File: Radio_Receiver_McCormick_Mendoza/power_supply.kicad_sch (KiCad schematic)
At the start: 27 parts, among them J1 VBAT, J2 GND, J23 VDDA, J26 +5V, J3 VA_3.3, J36 +5V RAW, J37 V_4.8, J39 VDD, J4 VA_4.8, J6 Conn_01x02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

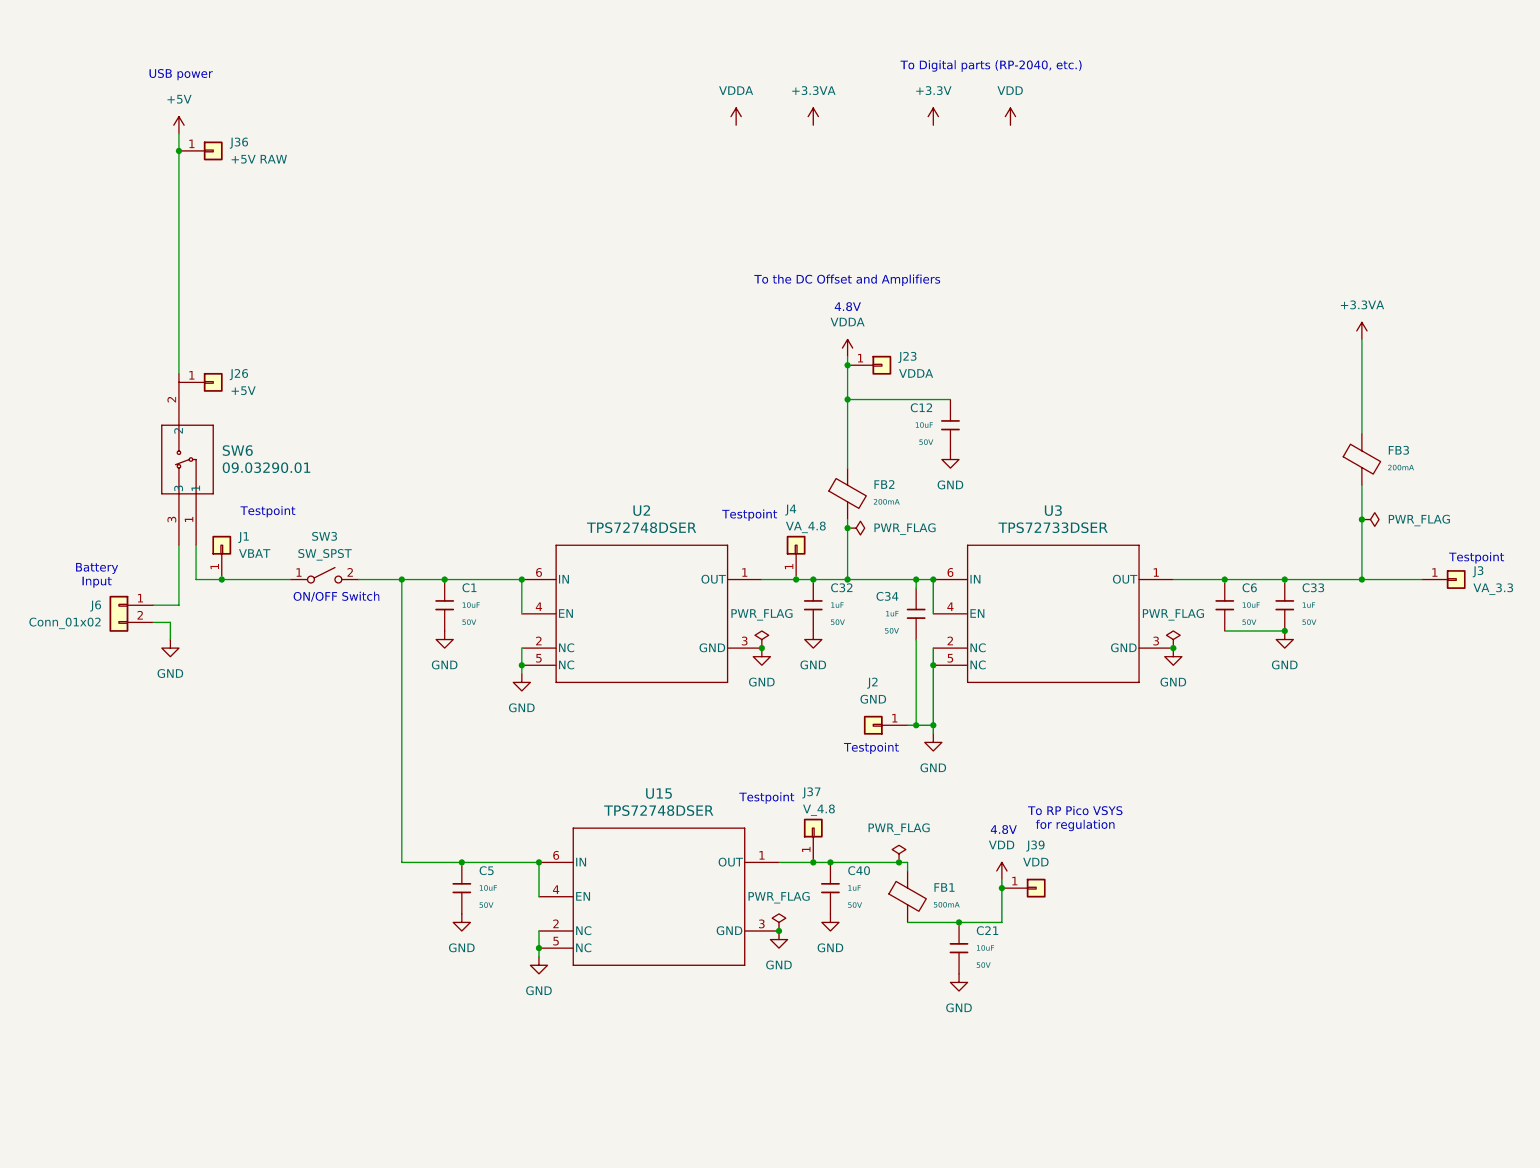
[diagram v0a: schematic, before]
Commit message: Integrated signal path modules
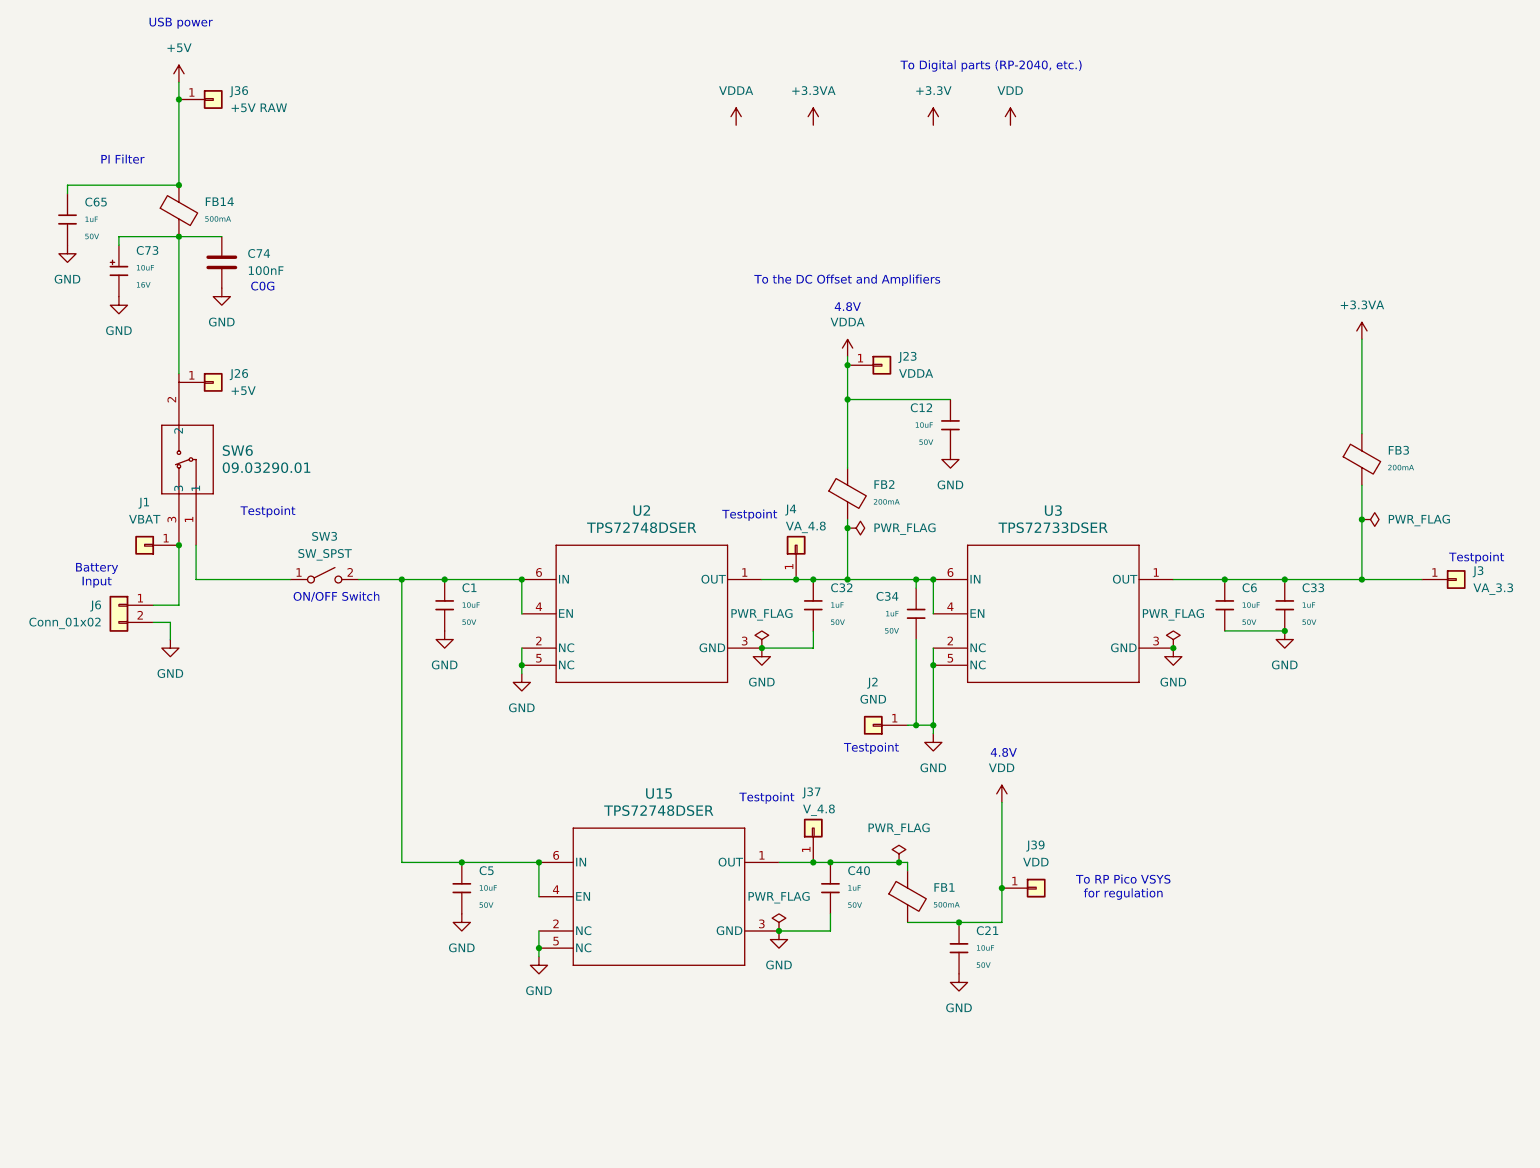
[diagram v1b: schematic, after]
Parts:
- added C65: 1uF, PCM_JLCPCB:C_0603, symbol PCM_JLCPCB-Capacitors:0603,1uF
- added C73: 10uF, PCM_JLCPCB:C_CASE-A-3216-18(mm), symbol PCM_JLCPCB-Capacitors:CASE-A-3216-18(mm),10uF
- added C74: 100nF, PCM_JLCPCB:C_1206, symbol Device:C
- added FB14: (no value), PCM_JLCPCB:FB_0805, symbol PCM_JLCPCB-Inductors:Ferrite,0805,(2)
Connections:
- net +5V: now also C65.1, FB14.1; no longer SW6.2
- net GND: now also C65.2, C73.2, C74.2
- net at J6.1 (Pin_1), SW6.3: now also J1.1 (Pin_1)
- net at SW3.1 (A), SW6.1: no longer J1.1 (Pin_1)
- new net: C73.1, C74.1, FB14.2, SW6.2
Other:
- note added: "C0G"
- note added: "PI Filter"
- moved on the sheet: J36

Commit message: Finalized Pico connections and added indicator LEDs
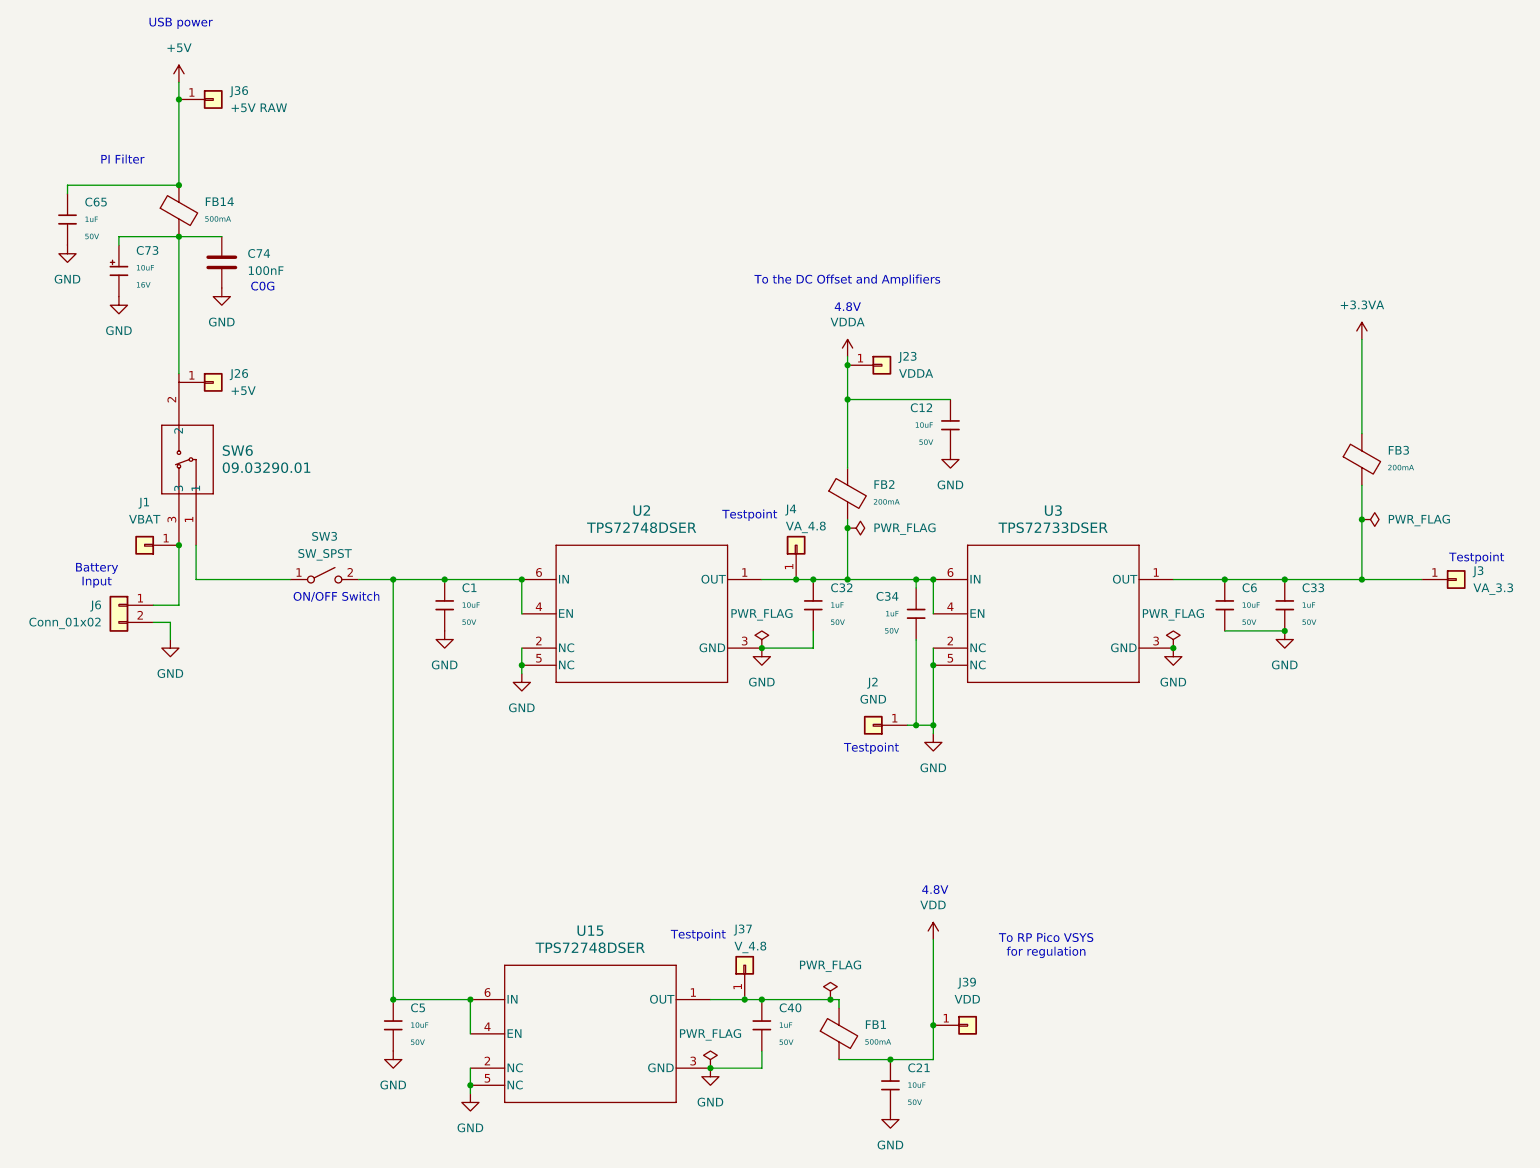
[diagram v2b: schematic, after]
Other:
- note removed: "To Digital parts (RP-2040, etc.)"
- moved on the sheet: C21, C40, C5, FB1, J37, J39, U15

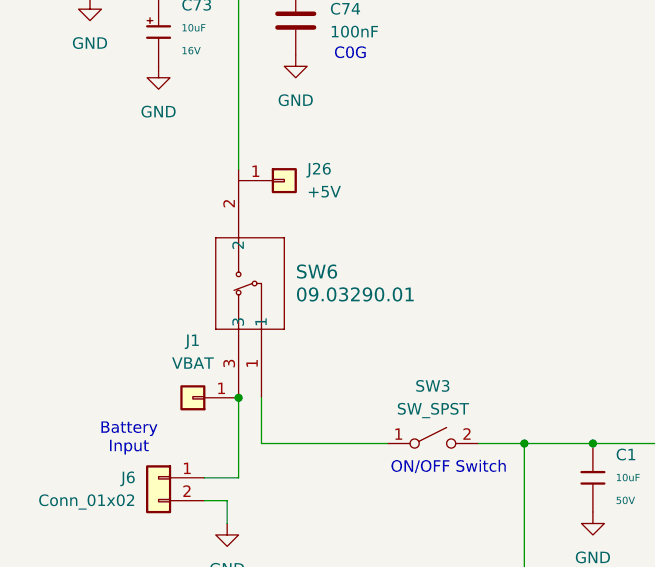
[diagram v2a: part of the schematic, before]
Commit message: Added transformer footprint and datasheet
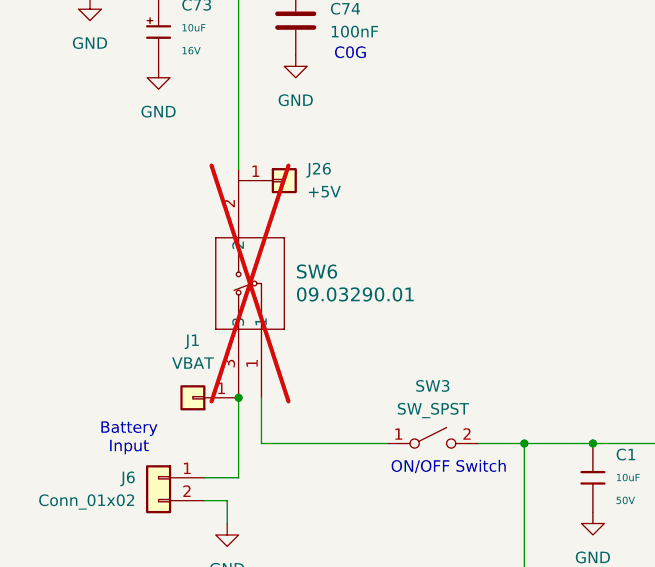
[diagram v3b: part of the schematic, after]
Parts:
- C65: Manufacturer Samsung Electro-Mechanics -> (none)
- C73: Manufacturer AVX -> (none)
- FB1, FB14: Manufacturer Sunlord -> (none)
- SW6: now not fitted
- U15, U2: LCSC (none) -> C2868088; Price (none) -> 4.374USD
- U3: LCSC (none) -> C544524; Price (none) -> 3.7957USD
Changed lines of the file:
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@@
 			)
 		)
-		(property "Manufacturer" "Sunlord"
-			(at 43.18 46.99 0)
-			(hide yes)
-			(show_name no)
-			(do_not_autoplace no)
-			(effects
-				(font
-					(size 1.27 1.27)
-				)
-			)
-		)
 		(property "Part" "GZ2012D601TF"
 			(at 43.18 46.99 0)
@@
 			)
 		)
-		(property "Manufacturer" "Samsung Electro-Mechanics"
-			(at 26.67 48.26 0)
-			(hide yes)
-			(show_name no)
-			(do_not_autoplace no)
-			(effects
-				(font
-					(size 1.27 1.27)
-				)
-			)
-		)
 		(property "Part" "CL10A105KB8NNNC"
 			(at 26.67 48.26 0)
@@
 			)
 		)
+		(property "LCSC" "C2868088"
+			(at 104.14 168.91 0)
+			(hide yes)
+			(show_name no)
+			(do_not_autoplace no)
+			(effects
+				(font
+					(size 1.27 1.27)
+				)
+			)
+		)
+		(property "Price" "4.374USD"
+			(at 104.14 168.91 0)
+			(hide yes)
+			(show_name no)
+			(do_not_autoplace no)
+			(effects
+				(font
+					(size 1.27 1.27)
+				)
+			)
+		)
 		(pin "1"
 		)
@@
 			)
 		)
-		(property "Manufacturer" "Sunlord"
-			(at 140.97 168.91 0)
-			(hide yes)
-			(show_name no)
-			(do_not_autoplace no)
-			(effects
-				(font
-					(size 1.27 1.27)
-				)
-			)
-		)
 		(property "Part" "GZ2012D601TF"
 			(at 140.97 168.91 0)
@@
 			)
 		)
+		(property "LCSC" "C2868088"
+			(at 111.76 106.68 0)
+			(hide yes)
+			(show_name no)
+			(do_not_autoplace no)
+			(effects
+				(font
+					(size 1.27 1.27)
+				)
+			)
+		)
+		(property "Price" "4.374USD"
+			(at 111.76 106.68 0)
+			(hide yes)
+			(show_name no)
+			(do_not_autoplace no)
+			(effects
+				(font
+					(size 1.27 1.27)
+				)
+			)
+		)
 		(pin "1"
 		)
@@
 		(on_board yes)
 		(in_pos_files yes)
-		(dnp no)
+		(dnp yes)
 		(fields_autoplaced yes)
 		(property "Reference" "SW6"
@@
 			)
 		)
-		(property "Manufacturer" "AVX"
-			(at 34.29 55.88 0)
-			(hide yes)
-			(show_name no)
-			(do_not_autoplace no)
-			(effects
-				(font
-					(size 1.27 1.27)
-				)
-			)
-		)
 		(property "Part" "TAJA106K016RNJ"
 			(at 34.29 55.88 0)
@@
 			(at 172.72 106.68 0)
 			(hide yes)
+			(show_name no)
+			(do_not_autoplace no)
+			(effects
+				(font
+					(size 1.27 1.27)
+				)
+			)
+		)
+		(property "LCSC" "C544524"
+			(at 172.72 106.68 0)
+			(hide yes)
+			(show_name no)
+			(do_not_autoplace no)
+			(effects
+				(font
+					(size 1.27 1.27)
+				)
+			)
+		)
+		(property "Price" "3.7957USD"
+			(at 172.72 106.68 0)
+			(hide yes)
